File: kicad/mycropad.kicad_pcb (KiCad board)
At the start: 2 copper layers, 116.2 x 64.8 mm, 21 parts, among them SW1 SW_Push, SW2 SW_Push, SW3 SW_Push, SW4 SW_Push, SW5 SW_Push, SW6 SW_Push, SW7 SW_Push, SW8 SW_Push, U1 Pico, U2 SN74AHCT125N

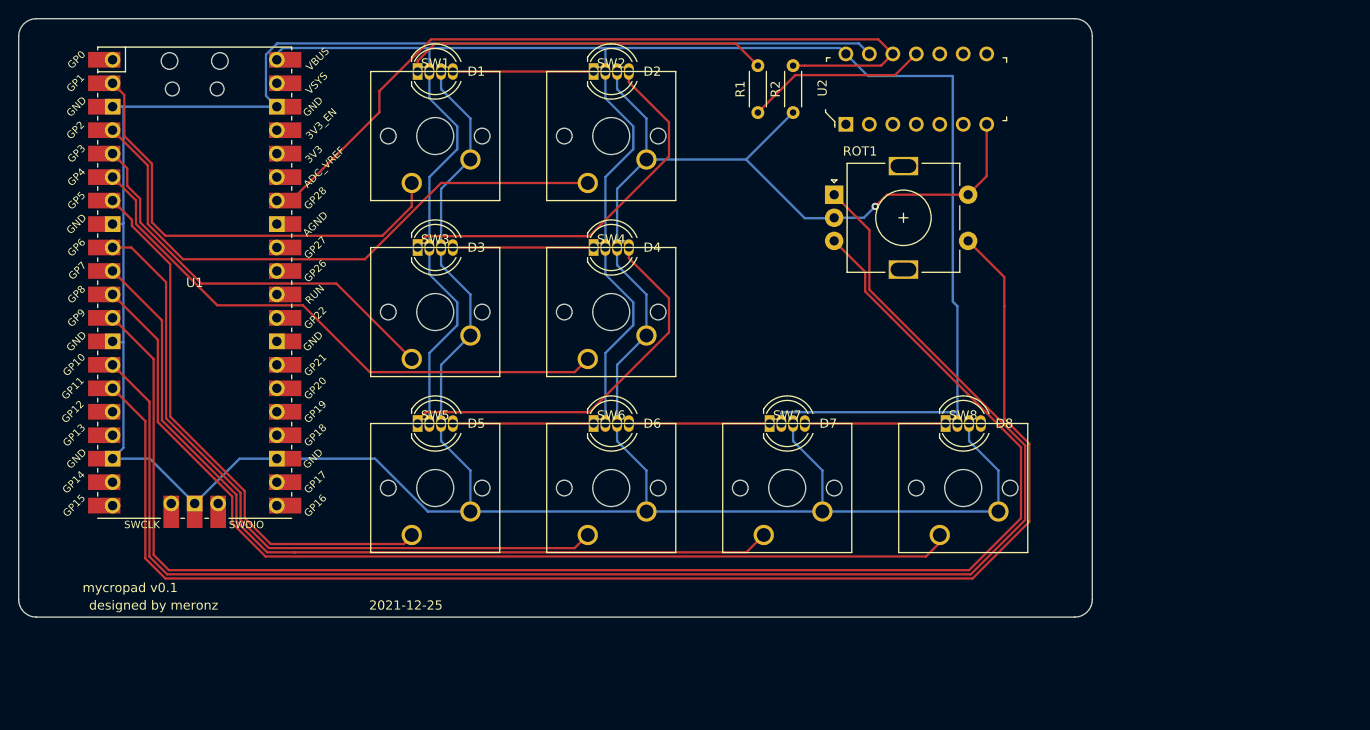
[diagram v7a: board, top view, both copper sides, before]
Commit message: Reinserted pcb mounting holes
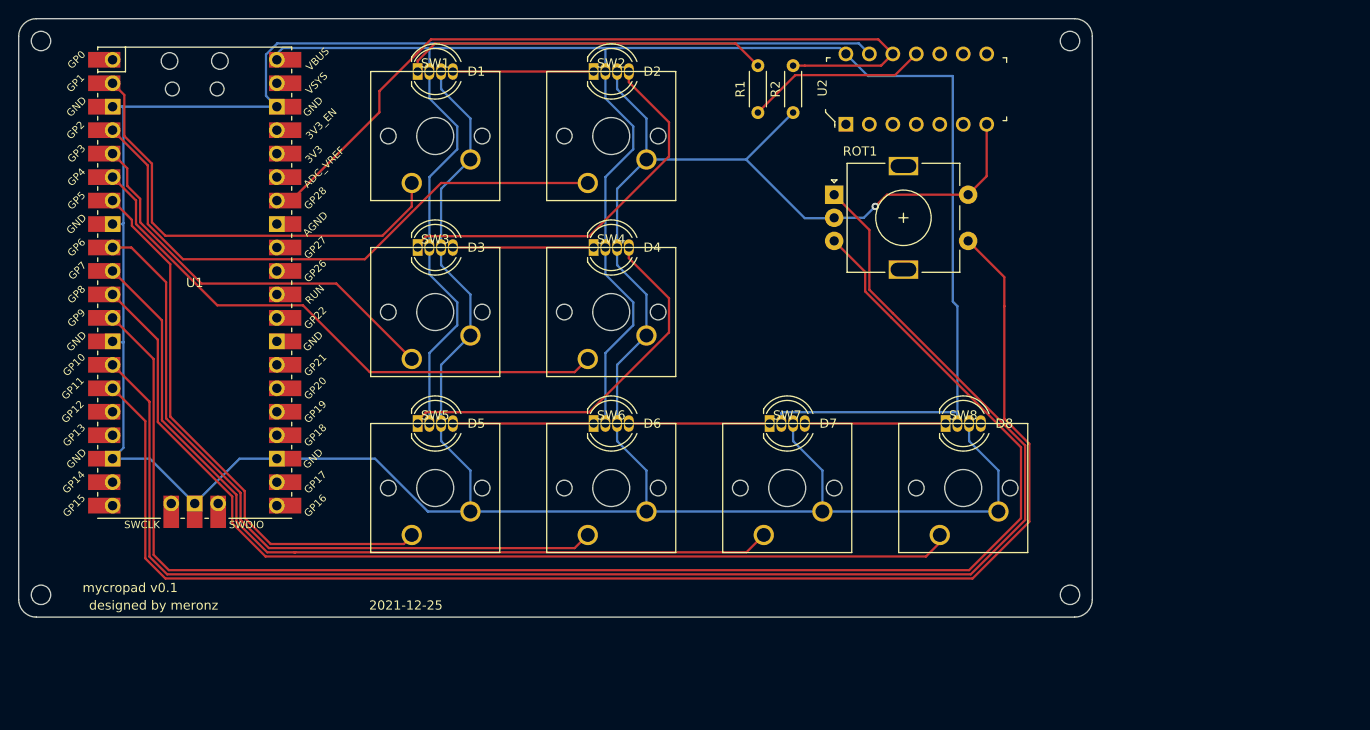
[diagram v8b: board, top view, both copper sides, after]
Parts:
- added REF**: MountingHole_2.1mm, MountingHole:MountingHole_2.1mm, F.Cu at (185.5, 65.9)
- added REF**: MountingHole_2.1mm, MountingHole:MountingHole_2.1mm, F.Cu at (185.5, 125.9)
- added REF**: MountingHole_2.1mm, MountingHole:MountingHole_2.1mm, F.Cu at (74.2, 125.9)
- added REF**: MountingHole_2.1mm, MountingHole:MountingHole_2.1mm, F.Cu at (74.2, 65.9)
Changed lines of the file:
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@@
     (tracks 242)
     (zones 0)
-    (modules 21)
+    (modules 25)
     (nets 57)
   )
@@
     (add_net "Net-(U2-Pad9)")
   )
+  (module MountingHole:MountingHole_2.1mm (layer F.Cu)
+    (at 185.547 65.913)
+    (descr "Mounting Hole 2.1mm, no annular")
+    (tags "mounting hole 2.1mm no annular")
+    (attr virtual)
+    (fp_text reference REF** (at 0 -3.2) (layer F.SilkS) hide
+      (effects (font (size 1 1) (thickness 0.15)))
+    )
+    (fp_text value MountingHole_2.1mm (at 0 3.2) (layer F.Fab) hide
+      (effects (font (size 1 1) (thickness 0.15)))
+    )
+    (fp_circle (center 0 0) (end 2.1 0) (layer Cmts.User) (width 0.15))
+    (fp_circle (center 0 0) (end 2.35 0) (layer F.CrtYd) (width 0.05))
+    (pad "" np_thru_hole circle (at 0 0) (size 2.1 2.1) (drill 2.1) (layers *.Cu *.Mask))
+  )
+  (module MountingHole:MountingHole_2.1mm (layer F.Cu)
+    (at 185.547 125.857)
+    (descr "Mounting Hole 2.1mm, no annular")
+    (tags "mounting hole 2.1mm no annular")
+    (attr virtual)
+    (fp_text reference REF** (at 0 -3.2) (layer F.SilkS) hide
+      (effects (font (size 1 1) (thickness 0.15)))
+    )
+    (fp_text value MountingHole_2.1mm (at 0 3.2) (layer F.Fab) hide
+      (effects (font (size 1 1) (thickness 0.15)))
+    )
+    (fp_circle (center 0 0) (end 2.1 0) (layer Cmts.User) (width 0.15))
+    (fp_circle (center 0 0) (end 2.35 0) (layer F.CrtYd) (width 0.05))
+    (pad "" np_thru_hole circle (at 0 0) (size 2.1 2.1) (drill 2.1) (layers *.Cu *.Mask))
+  )
+  (module MountingHole:MountingHole_2.1mm (layer F.Cu)
+    (at 74.168 125.857)
+    (descr "Mounting Hole 2.1mm, no annular")
+    (tags "mounting hole 2.1mm no annular")
+    (attr virtual)
+    (fp_text reference REF** (at 0 -3.2) (layer F.SilkS) hide
+      (effects (font (size 1 1) (thickness 0.15)))
+    )
+    (fp_text value MountingHole_2.1mm (at 0 3.2) (layer F.Fab) hide
+      (effects (font (size 1 1) (thickness 0.15)))
+    )
+    (fp_circle (center 0 0) (end 2.1 0) (layer Cmts.User) (width 0.15))
+    (fp_circle (center 0 0) (end 2.35 0) (layer F.CrtYd) (width 0.05))
+    (pad "" np_thru_hole circle (at 0 0) (size 2.1 2.1) (drill 2.1) (layers *.Cu *.Mask))
+  )
+  (module MountingHole:MountingHole_2.1mm (layer F.Cu)
+    (at 74.168 65.913)
+    (descr "Mounting Hole 2.1mm, no annular")
+    (tags "mounting hole 2.1mm no annular")
+    (attr virtual)
+    (fp_text reference REF** (at 0 -3.2) (layer F.SilkS) hide
+      (effects (font (size 1 1) (thickness 0.15)))
+    )
+    (fp_text value MountingHole_2.1mm (at 0 3.2) (layer F.Fab) hide
+      (effects (font (size 1 1) (thickness 0.15)))
+    )
+    (fp_circle (center 0 0) (end 2.1 0) (layer Cmts.User) (width 0.15))
+    (fp_circle (center 0 0) (end 2.35 0) (layer F.CrtYd) (width 0.05))
+    (pad "" np_thru_hole circle (at 0 0) (size 2.1 2.1) (drill 2.1) (layers *.Cu *.Mask))
+  )
   (module mycropad:RPi_Pico_SMD_TH (layer F.Cu)
     (at 90.805 92.075)
@@
     (arrow2b (pts (xy 147.87 85.72) (xy 147.283579 84.593496)))
   )
-  (dimension 111.125 (width 0.15) (layer F.Fab)
-    (gr_text "111.125 mm" (at 129.8575 55.85) (layer F.Fab)
-      (effects (font (size 1 1) (thickness 0.15)))
-    )
-    (feature1 (pts (xy 185.42 66.04) (xy 185.42 56.563579)))
-    (feature2 (pts (xy 74.295 66.04) (xy 74.295 56.563579)))
-    (crossbar (pts (xy 74.295 57.15) (xy 185.42 57.15)))
-    (arrow1a (pts (xy 185.42 57.15) (xy 184.293496 57.736421)))
-    (arrow1b (pts (xy 185.42 57.15) (xy 184.293496 56.563579)))
-    (arrow2a (pts (xy 74.295 57.15) (xy 75.421504 57.736421)))
-    (arrow2b (pts (xy 74.295 57.15) (xy 75.421504 56.563579)))
+  (dimension 111.379 (width 0.15) (layer F.Fab)
+    (gr_text "111.379 mm" (at 129.8575 55.723) (layer F.Fab)
+      (effects (font (size 1 1) (thickness 0.15)))
+    )
+    (feature1 (pts (xy 185.547 65.913) (xy 185.547 56.436579)))
+    (feature2 (pts (xy 74.168 65.913) (xy 74.168 56.436579)))
+    (crossbar (pts (xy 74.168 57.023) (xy 185.547 57.023)))
+    (arrow1a (pts (xy 185.547 57.023) (xy 184.420496 57.609421)))
+    (arrow1b (pts (xy 185.547 57.023) (xy 184.420496 56.436579)))
+    (arrow2a (pts (xy 74.168 57.023) (xy 75.294504 57.609421)))
+    (arrow2b (pts (xy 74.168 57.023) (xy 75.294504 56.436579)))
   )
   (gr_line (start 187.96 126.365) (end 187.96 65.405) (layer Edge.Cuts) (width 0.05))
@@
   (gr_arc (start 73.66 126.365) (end 71.755 126.365) (angle -90) (layer Edge.Cuts) (width 0.05))
   (gr_arc (start 73.66 65.405) (end 73.66 63.5) (angle -90) (layer Edge.Cuts) (width 0.05))
-  (dimension 59.69 (width 0.15) (layer F.Fab)
-    (gr_text "59.690 mm" (at 64.105 95.885 90) (layer F.Fab)
-      (effects (font (size 1 1) (thickness 0.15)))
-    )
-    (feature1 (pts (xy 74.295 66.04) (xy 64.818579 66.04)))
-    (feature2 (pts (xy 74.295 125.73) (xy 64.818579 125.73)))
-    (crossbar (pts (xy 65.405 125.73) (xy 65.405 66.04)))
-    (arrow1a (pts (xy 65.405 66.04) (xy 65.991421 67.166504)))
-    (arrow1b (pts (xy 65.405 66.04) (xy 64.818579 67.166504)))
-    (arrow2a (pts (xy 65.405 125.73) (xy 65.991421 124.603496)))
-    (arrow2b (pts (xy 65.405 125.73) (xy 64.818579 124.603496)))
-  )
-  (dimension 115.865 (width 0.15) (layer F.Fab)
-    (gr_text "115.865 mm" (at 130.0275 138.46) (layer F.Fab)
+  (dimension 59.944 (width 0.15) (layer F.Fab)
+    (gr_text "59.944 mm" (at 63.978 95.885 90) (layer F.Fab)
+      (effects (font (size 1 1) (thickness 0.15)))
+    )
+    (feature1 (pts (xy 74.168 65.913) (xy 64.691579 65.913)))
+    (feature2 (pts (xy 74.168 125.857) (xy 64.691579 125.857)))
+    (crossbar (pts (xy 65.278 125.857) (xy 65.278 65.913)))
+    (arrow1a (pts (xy 65.278 65.913) (xy 65.864421 67.039504)))
+    (arrow1b (pts (xy 65.278 65.913) (xy 64.691579 67.039504)))
+    (arrow2a (pts (xy 65.278 125.857) (xy 65.864421 124.730496)))
+    (arrow2b (pts (xy 65.278 125.857) (xy 64.691579 124.730496)))
+  )
+  (dimension 116.205 (width 0.15) (layer F.Fab)
+    (gr_text "116.205 mm" (at 129.8575 138.46) (layer F.Fab)
       (effects (font (size 1 1) (thickness 0.15)))
     )
     (feature1 (pts (xy 187.96 125.73) (xy 187.96 137.746421)))
-    (feature2 (pts (xy 72.095 125.73) (xy 72.095 137.746421)))
-    (crossbar (pts (xy 72.095 137.16) (xy 187.96 137.16)))
+    (feature2 (pts (xy 71.755 125.73) (xy 71.755 137.746421)))
+    (crossbar (pts (xy 71.755 137.16) (xy 187.96 137.16)))
     (arrow1a (pts (xy 187.96 137.16) (xy 186.833496 137.746421)))
     (arrow1b (pts (xy 187.96 137.16) (xy 186.833496 136.573579)))
-    (arrow2a (pts (xy 72.095 137.16) (xy 73.221504 137.746421)))
-    (arrow2b (pts (xy 72.095 137.16) (xy 73.221504 136.573579)))
+    (arrow2a (pts (xy 71.755 137.16) (xy 72.881504 137.746421)))
+    (arrow2b (pts (xy 71.755 137.16) (xy 72.881504 136.573579)))
   )
   (dimension 64.77 (width 0.15) (layer F.Fab)
